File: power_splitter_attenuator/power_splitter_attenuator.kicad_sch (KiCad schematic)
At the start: 40 parts, among them J1 SMA, J2 SMA, J3 SMA, J4 SMA, J5 SMA, J6 SMA, J7 SMA, J8 SMA

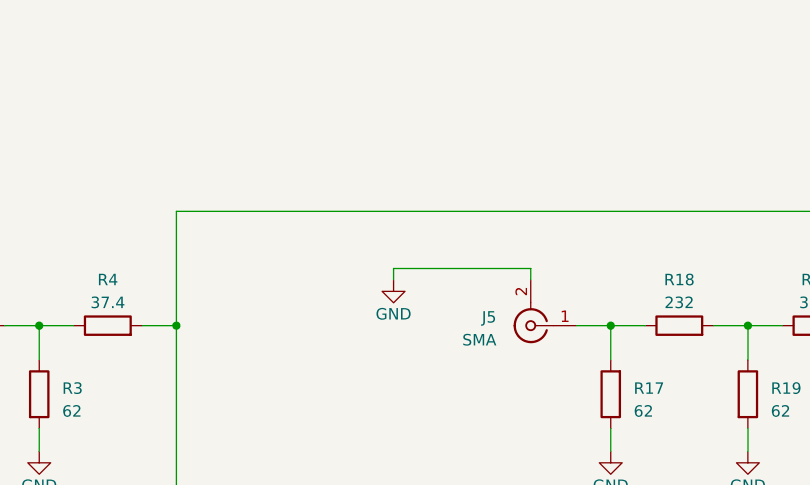
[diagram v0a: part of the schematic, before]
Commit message: power splitter: add PCB
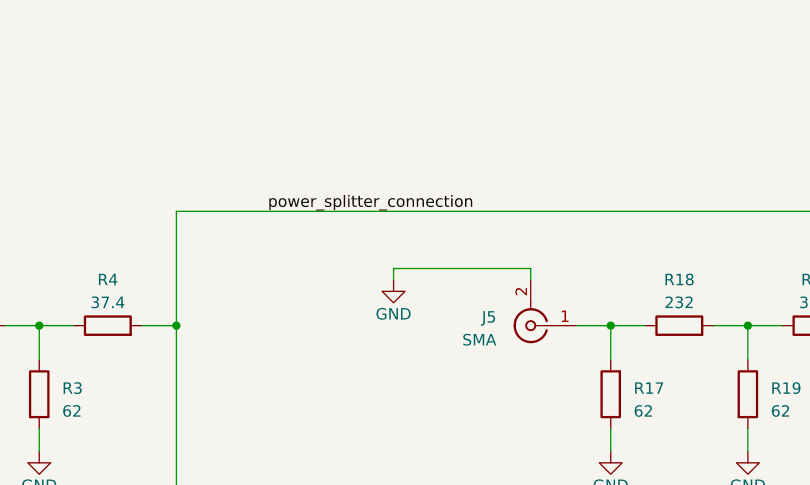
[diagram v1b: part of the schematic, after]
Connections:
- net power_splitter_connection: now reaches R12.2, R16.2, R20.2, R24.2, R28.2, R32.2, R4.2, R8.2
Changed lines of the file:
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@@
+    (effects (font (size 1.27 1.27)) (justify left bottom))
+  )
+  (label "power_splitter_connection" (at 127 36.83 0) (fields_autoplaced)
     (effects (font (size 1.27 1.27)) (justify left bottom))
   )

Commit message: power splitter: switch to SMA connector available at JLCPCB
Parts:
- J1, J2, J3, J4, J5, J6, J7, J8: Comment Alternative suitable part: Amphenol RF 901-10309 -> Alternative suitable part: Amphenol RF 901-10309, Johnson 1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; LCSC C9900004170 -> C1509221; LCSC Description (Global sourcing part) -> Inner bore SMA Board Edge Offset feet Plugin RF Connectors; MPN 142-0701-851 -> HJ-SMA076; Manufacturer Johnson -> HJ Tech

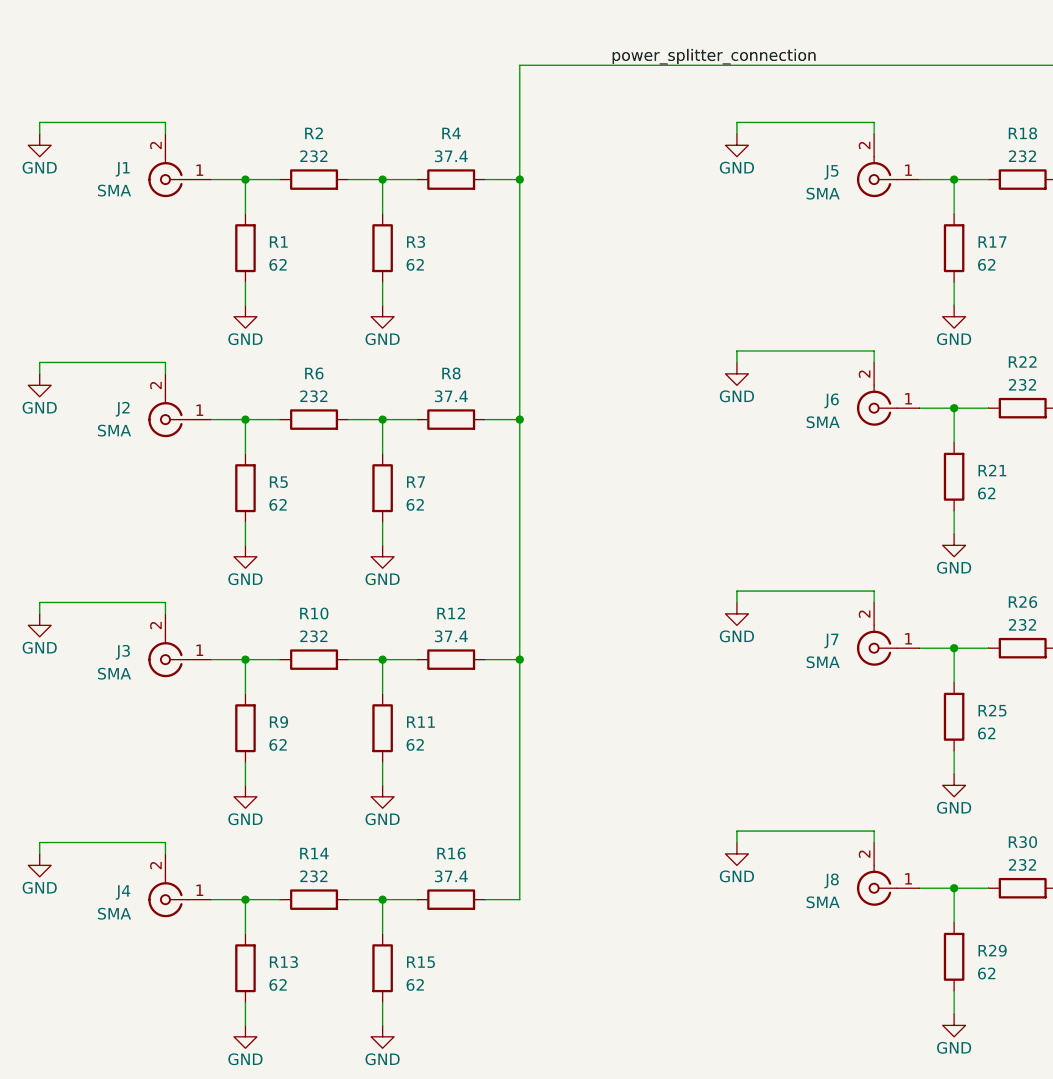
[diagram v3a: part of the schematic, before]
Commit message: power splitter attenuator: update files to KiCad 9
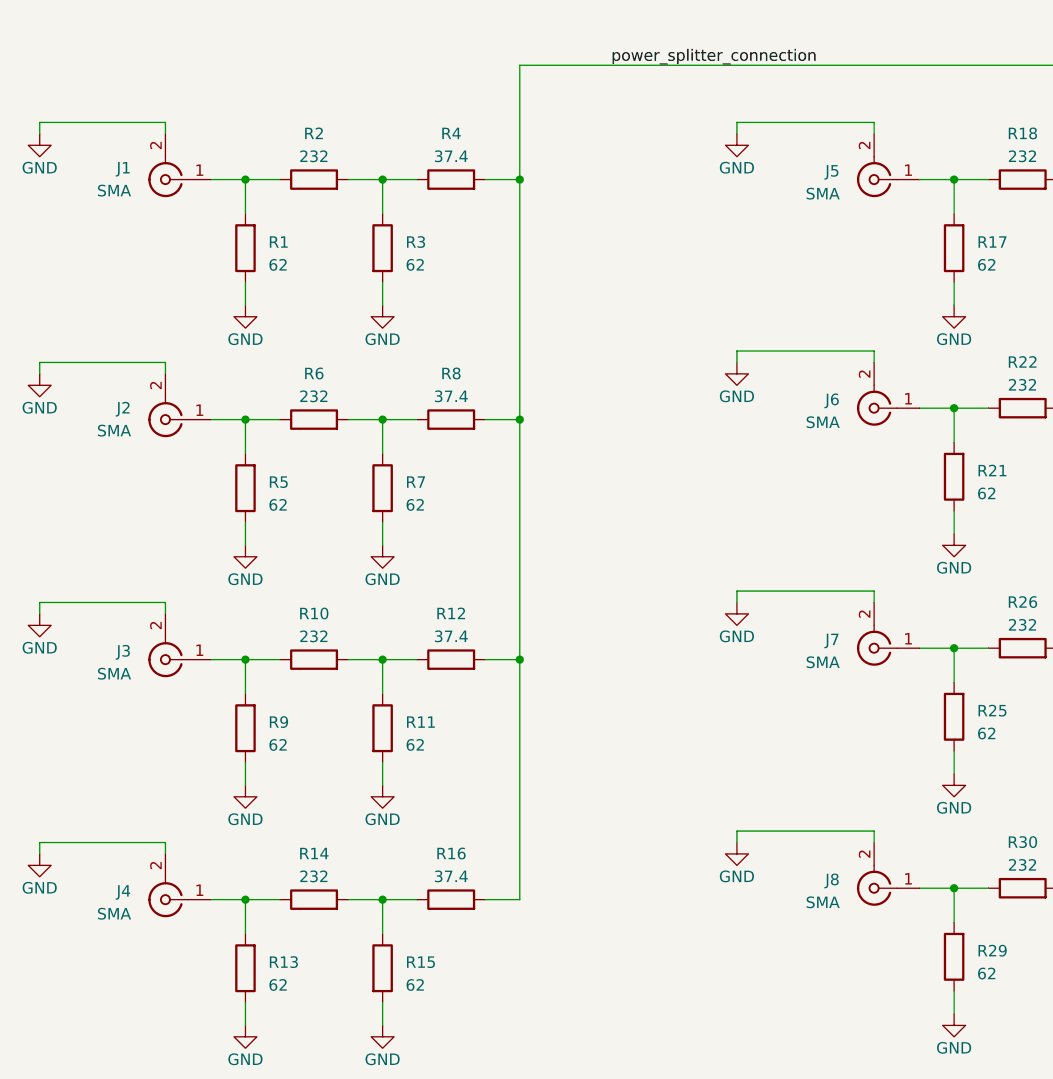
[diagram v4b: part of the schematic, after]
